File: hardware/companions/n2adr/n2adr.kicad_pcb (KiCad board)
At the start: 4 copper layers, 100 x 50 mm, 157 parts, among them J3 Conn_01x01, J4 Audio-Jack-2, K1 EC2-3NU, K2 EC2-3NU, K3 EC2-3NU, K4 EC2-3NU, K5 EC2-3NU, K6 EC2-3NU, K7 EC2-3NU, P1 TST, P10 SMA, P11 SMA, P12 Conn_01x20, P13 TST, P14 TST, P15 TST, P16 TST, P2 TST, P3 TST, P4 TST, P5 TST, P6 TST, P7 TST, P8 TST, P9 CONN_01X03, U1 MCP23008, U2 ULN2003LV, U3 AD8692, U5 74LVC1G00

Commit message: Updates to N2ADR board
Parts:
- added C12: 22uF, N2ADR:SMD_0805, B.Cu at (78.2, 59.2)
- added C15: 100uF, N2ADR:SMD-1206, B.Cu at (128.0, 57.2)
- added FB1: Ferrite_Bead_Small, N2ADR:SMD_0805, F.Cu at (116.0, 59.2)
- added R16: DNI, N2ADR:SMD_0805, B.Cu at (105.2, 97.1)
- C20, C27, C28, C29, C3, C30, C31, C5, C6: moved to B.Cu
- D3: moved to F.Cu
- P15: footprint Wire_Pads:SolderWirePad_single_0-8mmDrill -> N2ADR:SolderWirePad_single_0-8mmDrill
- moved REF** 24.5 mm to (151.0, 75.6)
- moved REF** 16.4 mm to (115.5, 66.2)
- moved REF** 11.3 mm to (108.0, 68.6)
- moved P3 11.2 mm to (109.9, 65.5)
- moved REF** 9.92 mm to (135.7, 65.5)
- moved REF** 6.91 mm to (107.3, 103.5)
- moved REF** 5.34 mm to (122.1, 75.0)
- moved C30 4.85 mm to (127.6, 60.5)
- moved REF** 4.80 mm to (143.8, 85.8)
- moved C20 4.52 mm to (74.5, 61.4)
- moved REF** 4.50 mm to (95.4, 65.3)
- moved C29 4.40 mm to (135.8, 71.1)
- moved REF** 3.94 mm to (103.2, 78.8)
- moved C2 3.52 mm to (132.6, 60.1), turned to 180 degrees
- moved C14 3.18 mm to (105.9, 81.1), turned to 270 degrees
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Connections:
- C14 pad 2: +3.3V -> +3V3
- C20 pad 2: +3.3V -> +3V3
- C27 pad 2: +3.3V -> +3V3
- C28 pad 2: +3.3V -> +3V3
- C29 pad 2: +3.3V -> +3V3
- C30 pad 2: +3.3V -> +3V3
- C31 pad 2: +3.3V -> +3V3
- C45 pad 2: +3.3V -> +3V3
- C50 pad 2: +3.3V -> +3V3
- C7 pad 2: +3.3V -> +3V3
- D3 pad 1: +3.3V -> +3V3
- K1 pad 1: +3.3V -> +3V3
- K2 pad 1: +3.3V -> +3V3
- K3 pad 1: +3.3V -> +3V3
- K4 pad 1: +3.3V -> +3V3
- K5 pad 1: +3.3V -> +3V3
- K6 pad 1: +3.3V -> +3V3
- K7 pad 1: +3.3V -> +3V3
- P12 pad 18: +3.3V -> Net-(FB1-Pad2)
- RV1 pad 3: (no net) -> Net-(RV1-Pad3)
- U1 pad 10: (no net) -> Net-(U1-Pad10)
- U1 pad 11: (no net) -> Net-(U1-Pad11)
- U1 pad 20: +3.3V -> +3V3
- U1 pad 6: +3.3V -> +3V3
- U1 pad 7: (no net) -> Net-(U1-Pad7)
- U1 pad 8: (no net) -> Net-(U1-Pad8)
- U2 pad 9: +3.3V -> +3V3
- U3 pad 8: +3.3V -> +3V3
- U5 pad 5: +3.3V -> +3V3
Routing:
- net +3V3: track 0.00 -> 247.1 mm, vias 0 -> 13
- net +3.3V: track 218.6 -> 0.00 mm, vias 6 -> 0
- net Net-(FB1-Pad2): track 0.00 -> 9.53 mm, vias 0 -> 1
- net Net-(R16-Pad2): track 7.05 -> 16.1 mm
- net Band6: track 54.5 -> 61.0 mm, vias 1 -> 2
- net Net-(K1-Pad6): track 17.5 -> 21.8 mm
- net Band2: track 44.7 -> 47.4 mm
- net INTTR: track 45.2 -> 47.6 mm, vias 2 -> 1
- net Net-(P12-Pad20): track 31.9 -> 34.2 mm
- net Net-(P12-Pad6): track 3.49 -> 4.90 mm
- net Band5: track 45.7 -> 44.5 mm
- net Band1: track 52.0 -> 50.9 mm
- net Band4: track 37.6 -> 38.6 mm
- net Net-(J4-Pad1): track 67.1 -> 66.1 mm
- net Net-(P13-Pad1): track 10.9 -> 10.1 mm
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
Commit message: Finalizing n2adr changes
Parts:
- added REF**: via, Local:via30, F.Cu at (138.8, 86.2)
- moved REF** 49.9 mm to (95.4, 69.6)
- moved REF** 2.82 mm to (131.6, 89.8)
- moved REF** 2.03 mm to (102.1, 94.8)
- moved P10 1.80 mm to (129.0, 102.7)
- moved P11 1.80 mm to (97.0, 102.7)
- moved R15 0.70 mm to (123.0, 95.9)
- moved R14 0.60 mm to (128.5, 95.9)
- moved C7 0.30 mm to (123.0, 93.5)
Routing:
- net GND: track 14.3 -> 28.1 mm, vias 1 -> 2
- net +3V3: track 247.1 -> 249.1 mm
- net Net-(R14-Pad2): track 6.46 -> 5.82 mm
- net Net-(R13-Pad2): track 10.3 -> 9.70 mm
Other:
- outline, holes or cut-outs redrawn
- board text added: "Hermes Lite 2 Filters Rev E5 © 2018 by N2ADR"
- board text removed: "Hermes Lite 2 Filters Rev E4 © 2018 by N2ADR"

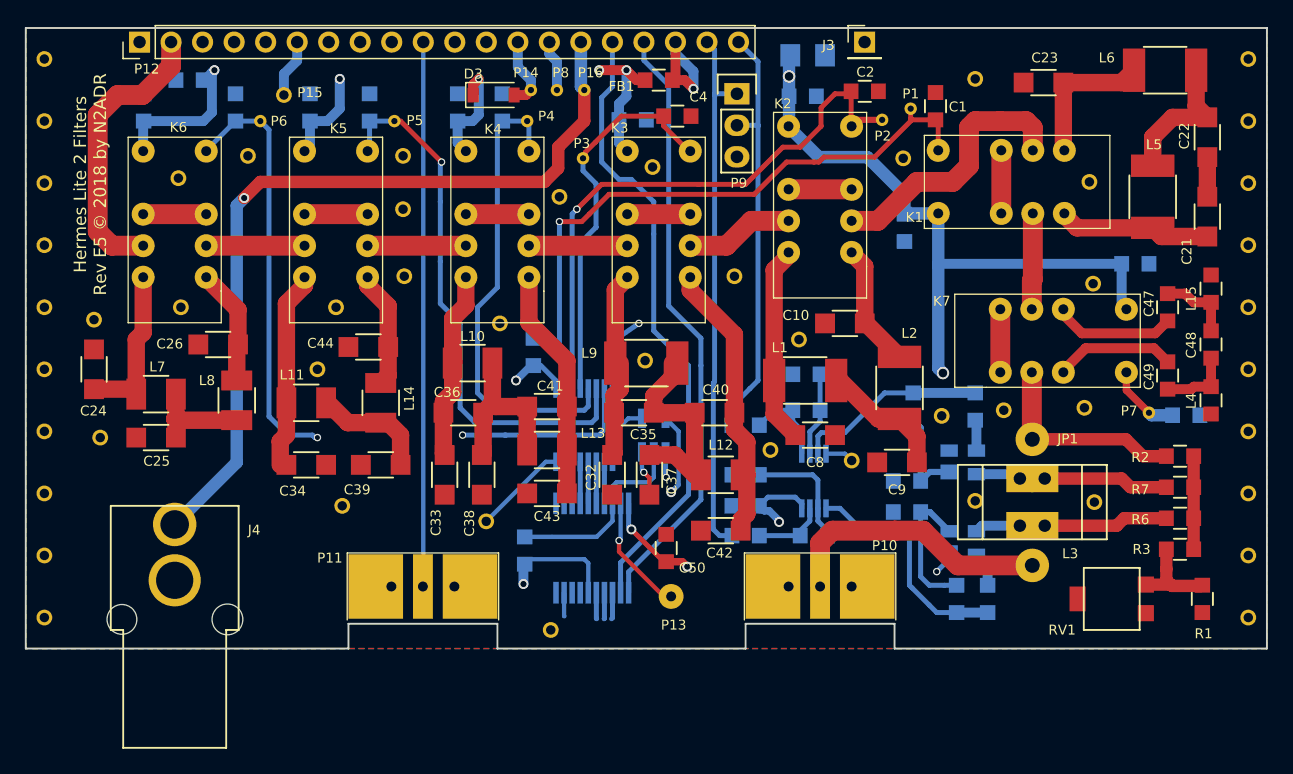
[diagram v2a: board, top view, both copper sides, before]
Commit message: Sync PCB with schematic
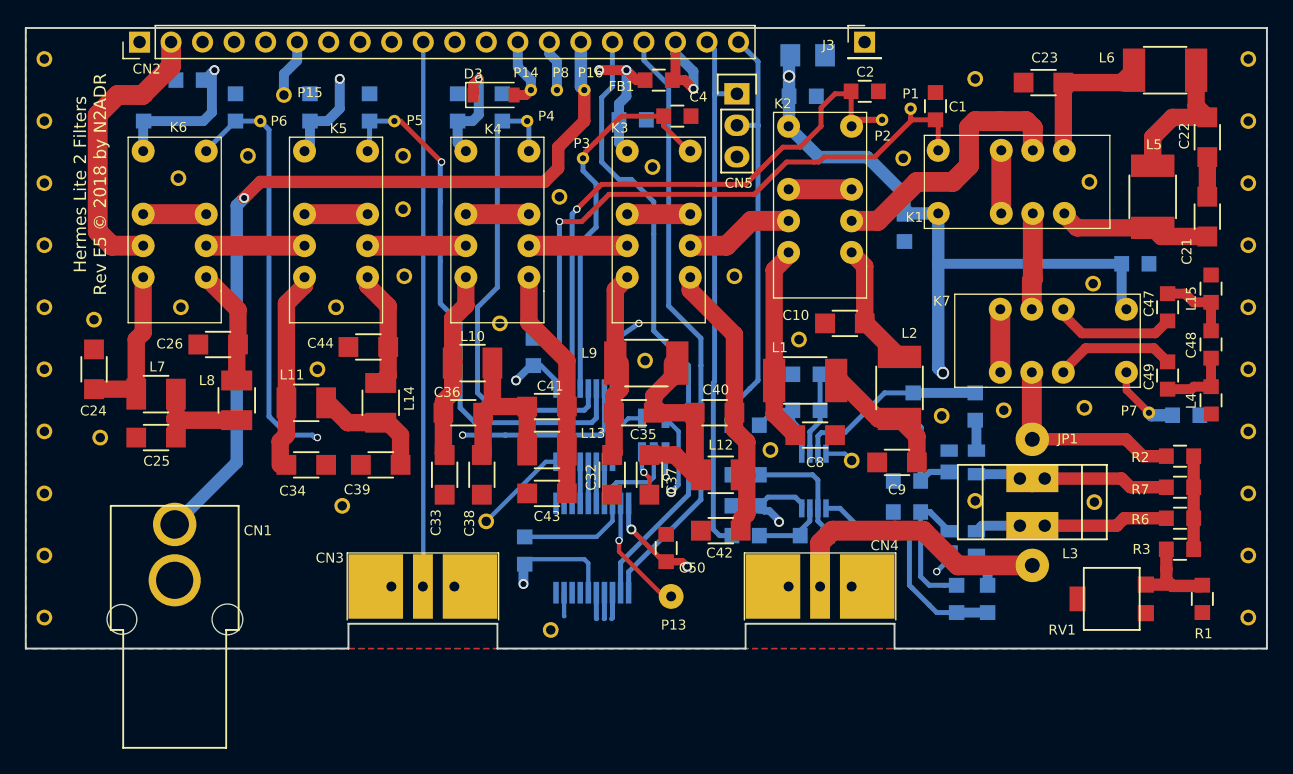
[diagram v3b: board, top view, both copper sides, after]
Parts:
- FB1: value Ferrite_Bead_Small -> FB
- renumbered J4 to CN1, P12 to CN2, P11 to CN3, P10 to CN4, P9 to CN5
